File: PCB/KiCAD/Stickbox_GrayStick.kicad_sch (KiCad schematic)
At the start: 11 parts, among them U1 MCP3002, U10 DRV5055A2xDBZxQ1, U11 DRV5055A2xDBZxQ1, U2 Stickbox_Assembly_Main

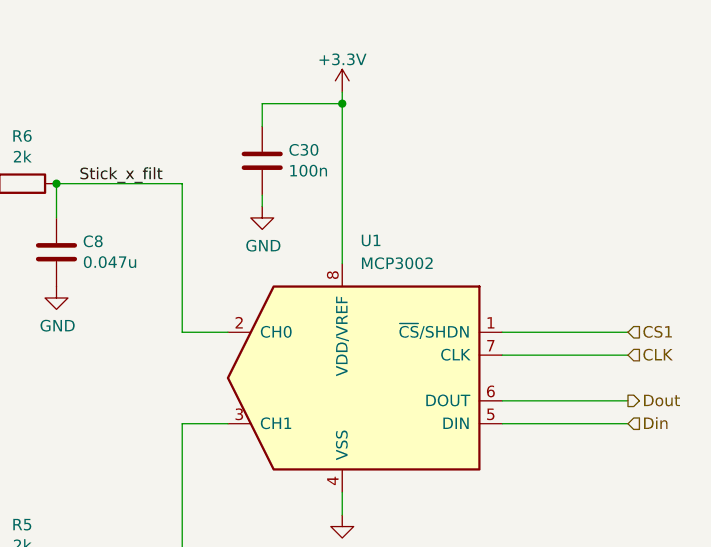
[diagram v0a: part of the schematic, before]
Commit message: Assembly and fab upload
Upload schematic pdf and bom csv and ibom html docs
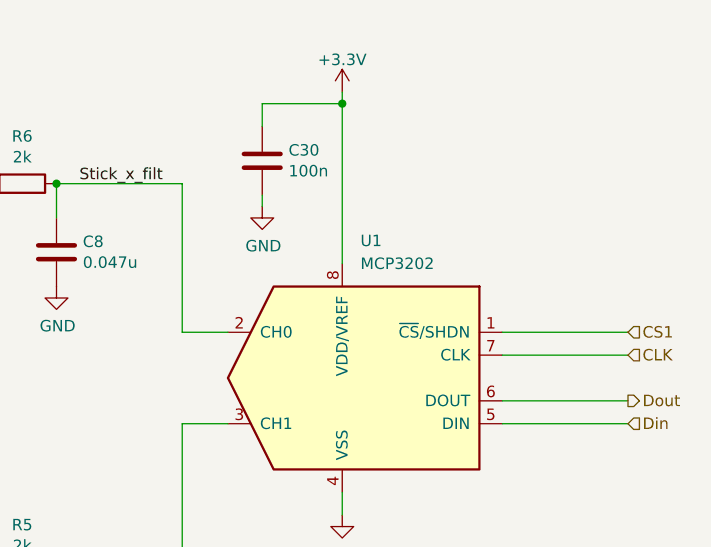
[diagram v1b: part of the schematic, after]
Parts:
- C11, C12: MPN (none) -> CL10B104KB8NNWC; Manufacturer (none) -> Samsung Electro-Mechanics; Package (none) -> 0603; VARIANT (none) -> NoVar
- C30: MPN (none) -> CL05B104KA5NNNC; Manufacturer (none) -> Samsung Electro-Mechanics; Package (none) -> 0402; VARIANT (none) -> NoVar
- C6, C8: MPN (none) -> CL10B473KB8NNNC; Manufacturer (none) -> Samsung Electro-Mechanics; Package (none) -> 0603; VARIANT (none) -> NoVar
- R5, R6: MPN (none) -> RC0603FR-132KL; Manufacturer (none) -> YAGEO; Package (none) -> 0603; VARIANT (none) -> NoVar
- U1: value MCP3002 -> MCP3202; MPN (none) -> MCP3202-CI/SN; Manufacturer (none) -> Microchip Technology; Package (none) -> 8-SOIC; VARIANT (none) -> NoVar
- U10, U11: LCSC (none) -> C266128; MPN (none) -> DRV5055A3QDBZR; Manufacturer (none) -> Texas Instruments; Package (none) -> SOT-23; VARIANT (none) -> NoVar
- U2: MPN (none) -> T3+Magnet_Assy; Manufacturer (none) -> Internal; Package (none) -> Through-hole; VARIANT (none) -> NoVar
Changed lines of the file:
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@@
       (effects (font (size 1.27 1.27)) (justify left))
     )
-    (property "Value" "MCP3002" (id 1) (at 198.8694 82.55 0)
+    (property "Value" "MCP3202" (id 1) (at 198.8694 82.55 0)
       (effects (font (size 1.27 1.27)) (justify left))
     )
@@
     )
     (property "Datasheet" "http://ww1.microchip.com/downloads/en/DeviceDoc/21294E.pdf" (id 3) (at 196.85 90.17 0)
+      (effects (font (size 1.27 1.27)) hide)
+    )
+    (property "Package" "8-SOIC" (id 4) (at 196.85 95.25 0)
+      (effects (font (size 1.27 1.27)) hide)
+    )
+    (property "MPN" "MCP3202-CI/SN" (id 5) (at 196.85 95.25 0)
+      (effects (font (size 1.27 1.27)) hide)
+    )
+    (property "Manufacturer" "Microchip Technology" (id 6) (at 196.85 95.25 0)
+      (effects (font (size 1.27 1.27)) hide)
+    )
+    (property "VARIANT" "NoVar" (id 7) (at 196.85 95.25 0)
       (effects (font (size 1.27 1.27)) hide)
     )
@@
       (effects (font (size 1.27 1.27)) hide)
     )
-    (property "MPN" "" (id 5) (at 165.1 81.28 0)
-      (effects (font (size 1.27 1.27)) hide)
-    )
-    (property "Manufacturer" "" (id 6) (at 165.1 81.28 0)
+    (property "MPN" "CL10B473KB8NNNC" (id 5) (at 165.1 81.28 0)
+      (effects (font (size 1.27 1.27)) hide)
+    )
+    (property "Manufacturer" "Samsung Electro-Mechanics" (id 6) (at 165.1 81.28 0)
+      (effects (font (size 1.27 1.27)) hide)
+    )
+    (property "Package" "0603" (id 7) (at 165.1 81.28 0)
+      (effects (font (size 1.27 1.27)) hide)
+    )
+    (property "VARIANT" "NoVar" (id 8) (at 165.1 81.28 0)
       (effects (font (size 1.27 1.27)) hide)
     )
@@
       (effects (font (size 1.27 1.27)) hide)
     )
+    (property "MPN" "DRV5055A3QDBZR" (id 4) (at 128.27 73.66 0)
+      (effects (font (size 1.27 1.27)) hide)
+    )
+    (property "Manufacturer" "Texas Instruments" (id 5) (at 128.27 73.66 0)
+      (effects (font (size 1.27 1.27)) hide)
+    )
+    (property "Package" "SOT-23" (id 6) (at 128.27 73.66 0)
+      (effects (font (size 1.27 1.27)) hide)
+    )
+    (property "LCSC" "C266128" (id 7) (at 128.27 73.66 0)
+      (effects (font (size 1.27 1.27)) hide)
+    )
+    (property "VARIANT" "NoVar" (id 8) (at 128.27 73.66 0)
+      (effects (font (size 1.27 1.27)) hide)
+    )
     (pin "1")
     (pin "2")
@@
       (effects (font (size 1.27 1.27)) hide)
     )
+    (property "MPN" "CL05B104KA5NNNC" (id 4) (at 187.96 71.12 0)
+      (effects (font (size 1.27 1.27)) hide)
+    )
+    (property "Manufacturer" "Samsung Electro-Mechanics" (id 5) (at 187.96 71.12 0)
+      (effects (font (size 1.27 1.27)) hide)
+    )
+    (property "Package" "0402" (id 6) (at 187.96 71.12 0)
+      (effects (font (size 1.27 1.27)) hide)
+    )
+    (property "VARIANT" "NoVar" (id 7) (at 187.96 71.12 0)
+      (effects (font (size 1.27 1.27)) hide)
+    )
     (pin "1")
     (pin "2")
@@
       (effects (font (size 1.27 1.27)) hide)
     )
+    (property "MPN" "DRV5055A3QDBZR" (id 4) (at 128.27 116.84 0)
+      (effects (font (size 1.27 1.27)) hide)
+    )
+    (property "Manufacturer" "Texas Instruments" (id 5) (at 128.27 116.84 0)
+      (effects (font (size 1.27 1.27)) hide)
+    )
+    (property "Package" "SOT-23" (id 6) (at 128.27 116.84 0)
+      (effects (font (size 1.27 1.27)) hide)
+    )
+    (property "LCSC" "C266128" (id 7) (at 128.27 116.84 0)
+      (effects (font (size 1.27 1.27)) hide)
+    )
+    (property "VARIANT" "NoVar" (id 8) (at 128.27 116.84 0)
+      (effects (font (size 1.27 1.27)) hide)
+    )
     (pin "1")
     (pin "2")
@@
     )
     (property "Datasheet" "" (id 3) (at 88.9 116.84 0)
+      (effects (font (size 1.27 1.27)) hide)
+    )
+    (property "MPN" "T3+Magnet_Assy" (id 4) (at 88.9 83.82 0)
+      (effects (font (size 1.27 1.27)) hide)
+    )
+    (property "Package" "Through-hole" (id 5) (at 88.9 83.82 0)
+      (effects (font (size 1.27 1.27)) hide)
+    )
+    (property "Manufacturer" "Internal" (id 6) (at 88.9 83.82 0)
+      (effects (font (size 1.27 1.27)) hide)
+    )
+    (property "VARIANT" "NoVar" (id 7) (at 88.9 83.82 0)
       (effects (font (size 1.27 1.27)) hide)
     )
@@
       (effects (font (size 1.27 1.27)) hide)
     )
-    (property "MPN" "" (id 5) (at 165.1 124.46 0)
-      (effects (font (size 1.27 1.27)) hide)
-    )
-    (property "Manufacturer" "" (id 6) (at 165.1 124.46 0)
+    (property "MPN" "CL10B473KB8NNNC" (id 5) (at 165.1 124.46 0)
+      (effects (font (size 1.27 1.27)) hide)
+    )
+    (property "Manufacturer" "Samsung Electro-Mechanics" (id 6) (at 165.1 124.46 0)
+      (effects (font (size 1.27 1.27)) hide)
+    )
+    (property "Package" "0603" (id 7) (at 165.1 124.46 0)
+      (effects (font (size 1.27 1.27)) hide)
+    )
+    (property "VARIANT" "NoVar" (id 8) (at 165.1 124.46 0)
       (effects (font (size 1.27 1.27)) hide)
     )
@@
       (effects (font (size 1.27 1.27)) hide)
     )
-    (property "MPN" "" (id 5) (at 114.3 110.49 0)
-      (effects (font (size 1.27 1.27)) hide)
-    )
-    (property "Manufacturer" "" (id 6) (at 114.3 110.49 0)
+    (property "MPN" "CL10B104KB8NNWC" (id 5) (at 114.3 110.49 0)
+      (effects (font (size 1.27 1.27)) hide)
+    )
+    (property "Manufacturer" "Samsung Electro-Mechanics" (id 6) (at 114.3 110.49 0)
+      (effects (font (size 1.27 1.27)) hide)
+    )
+    (property "Package" "0603" (id 7) (at 114.3 110.49 0)
+      (effects (font (size 1.27 1.27)) hide)
+    )
+    (property "VARIANT" "NoVar" (id 8) (at 114.3 110.49 0)
       (effects (font (size 1.27 1.27)) hide)
     )
@@
       (effects (font (size 1.27 1.27)) hide)
     )
-    (property "MPN" "" (id 5) (at 113.03 67.31 0)
-      (effects (font (size 1.27 1.27)) hide)
-    )
-    (property "Manufacturer" "" (id 6) (at 113.03 67.31 0)
+    (property "MPN" "CL10B104KB8NNWC" (id 5) (at 113.03 67.31 0)
+      (effects (font (size 1.27 1.27)) hide)
+    )
+    (property "Manufacturer" "Samsung Electro-Mechanics" (id 6) (at 113.03 67.31 0)
+      (effects (font (size 1.27 1.27)) hide)
+    )
+    (property "Package" "0603" (id 7) (at 113.03 67.31 0)
+      (effects (font (size 1.27 1.27)) hide)
+    )
+    (property "VARIANT" "NoVar" (id 8) (at 113.03 67.31 0)
       (effects (font (size 1.27 1.27)) hide)
     )
@@
       (effects (font (size 1.27 1.27)) hide)
     )
-    (property "MPN" "" (id 5) (at 161.29 73.66 0)
-      (effects (font (size 1.27 1.27)) hide)
-    )
-    (property "Manufacturer" "" (id 6) (at 161.29 73.66 0)
+    (property "MPN" "RC0603FR-132KL" (id 5) (at 161.29 73.66 0)
+      (effects (font (size 1.27 1.27)) hide)
+    )
+    (property "Manufacturer" "YAGEO" (id 6) (at 161.29 73.66 0)
+      (effects (font (size 1.27 1.27)) hide)
+    )
+    (property "Package" "0603" (id 7) (at 161.29 73.66 0)
+      (effects (font (size 1.27 1.27)) hide)
+    )
+    (property "VARIANT" "NoVar" (id 8) (at 161.29 73.66 0)
       (effects (font (size 1.27 1.27)) hide)
     )
@@
       (effects (font (size 1.27 1.27)) hide)
     )
-    (property "MPN" "" (id 5) (at 161.29 116.84 0)
-      (effects (font (size 1.27 1.27)) hide)
-    )
-    (property "Manufacturer" "" (id 6) (at 161.29 116.84 0)
-      (effects (font (size 1.27 1.27)) hide)
-    )
+    (property "MPN" "RC0603FR-132KL" (id 5) (at 161.29 116.84 0)
+      (effects (font (size 1.27 1.27)) hide)
+    )
+    (property "Manufacturer" "YAGEO" (id 6) (at 161.29 116.84 0)
+      (effects (font (size 1.27 1.27)) hide)
+    )
+    (property "Package" "0603" (id 7) (at 161.29 116.84 0)
+      (effects (font (size 1.27 1.27)) hide)
+    )
+    (property "VARIANT" "NoVar" (id 8) (at 161.29 116.84 0)
+      (effects (font (size 1.27 1.27)) hide)
+    )
